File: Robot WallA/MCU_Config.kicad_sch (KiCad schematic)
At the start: 26 parts, among them SW1 Switch

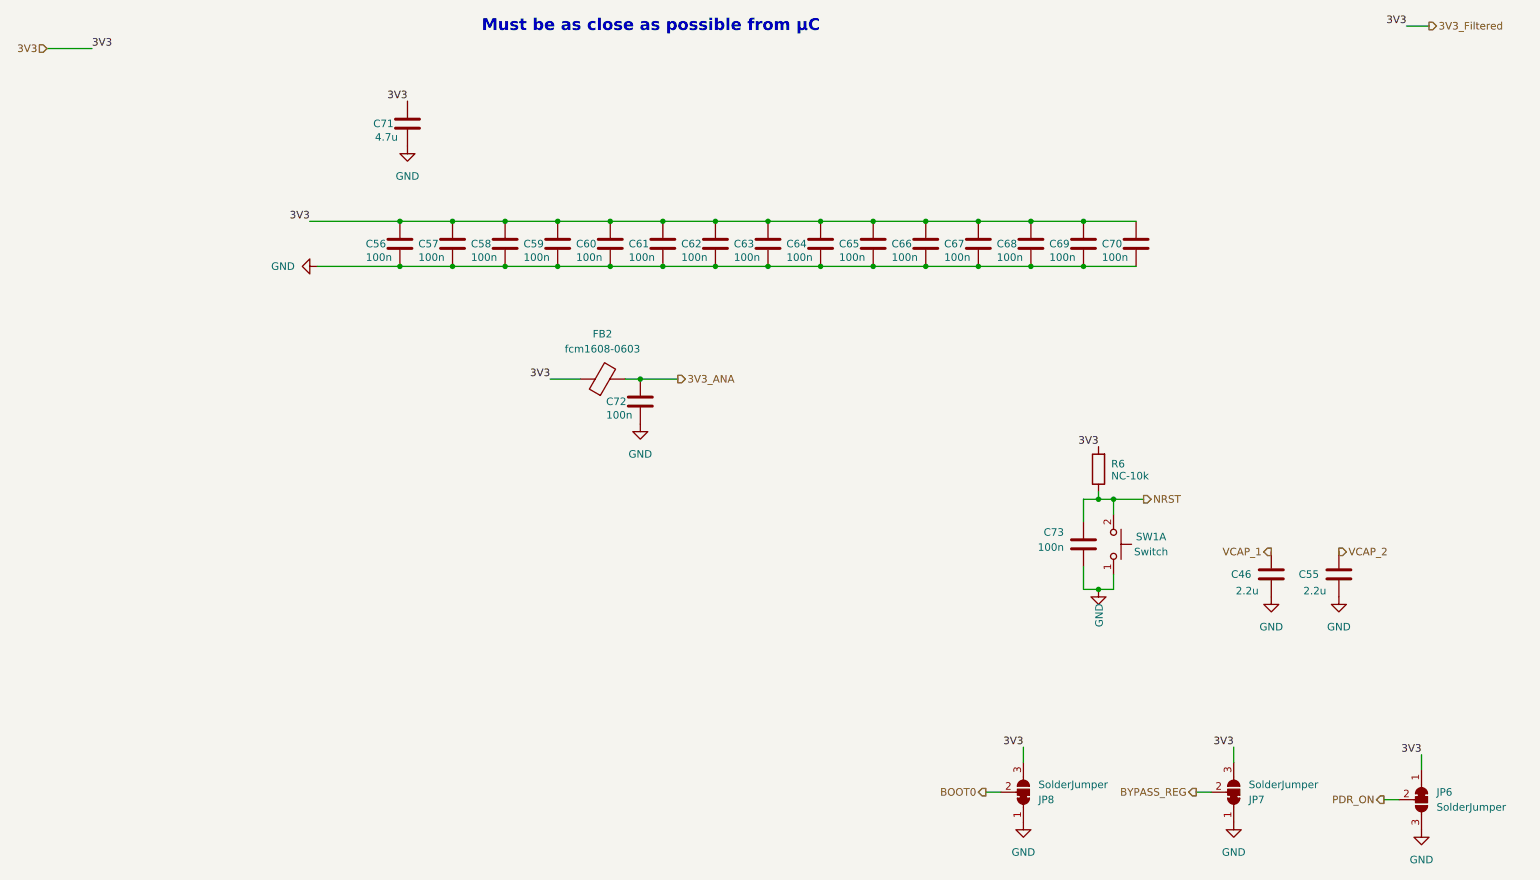
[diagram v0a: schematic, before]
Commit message: Continued to link MCU pins, Added a sheet for servomotors and optional 2 DC motors.
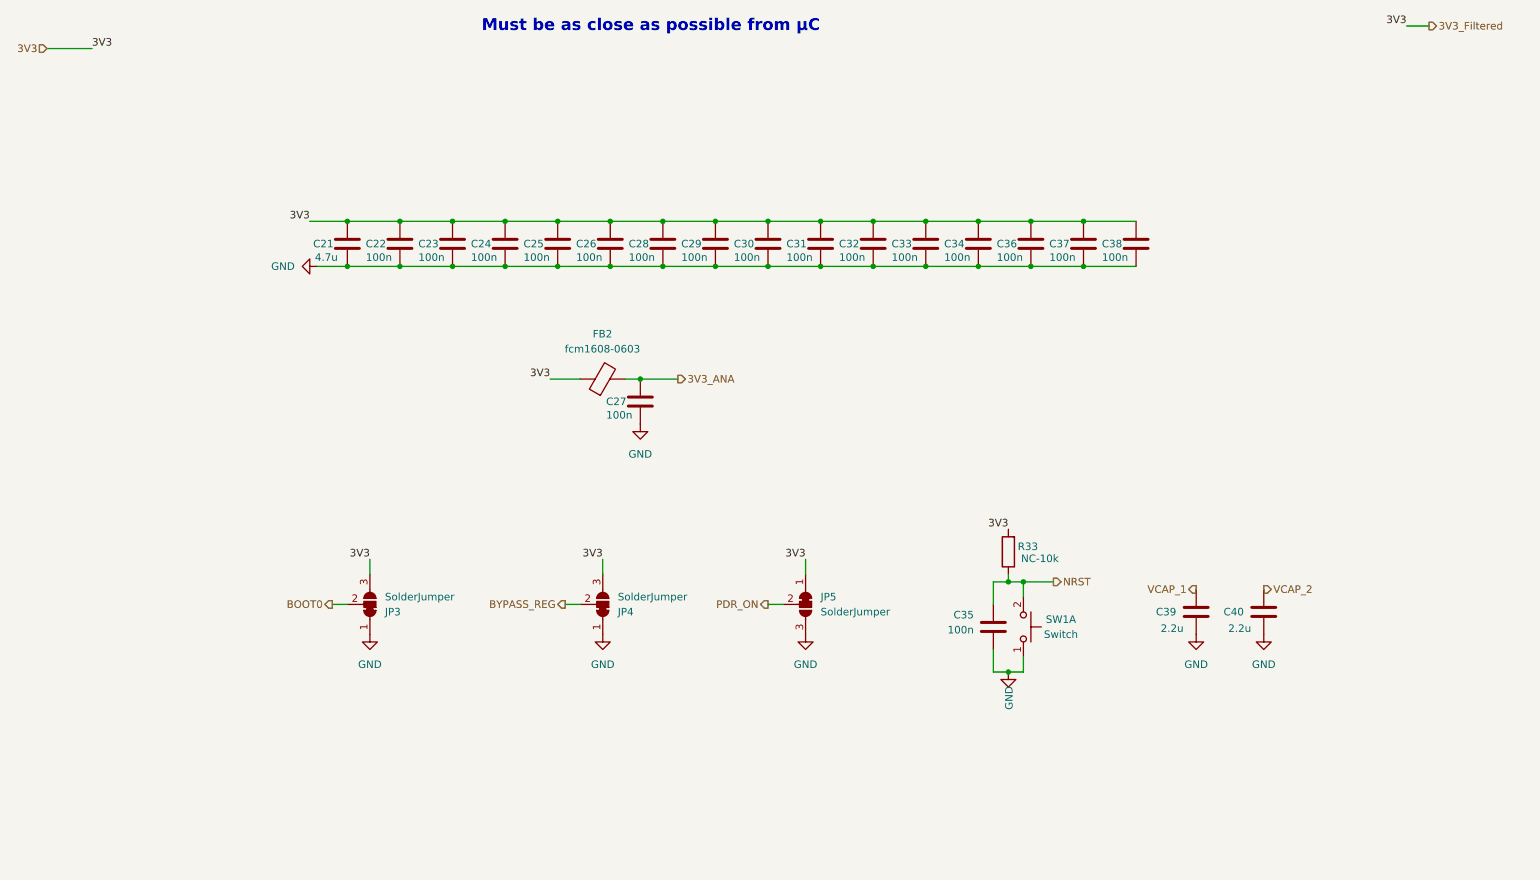
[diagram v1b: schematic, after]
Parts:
- renumbered C71 to C21, C56 to C22, C57 to C23, C58 to C24, C59 to C25, C60 to C26, C72 to C27, C61 to C28, C62 to C29, C63 to C30, C64 to C31, C65 to C32, C66 to C33, C67 to C34, C73 to C35, C68 to C36, C69 to C37, C70 to C38, C46 to C39, C55 to C40, JP8 to JP3, JP7 to JP4, JP6 to JP5, R6 to R33
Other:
- moved on the sheet: C21, C35, C39, C40, JP3, JP4, JP5, R33, SW1A

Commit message: Defined every footprints
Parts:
- C10: renamed from C29; value 100n -> 100nF; footprint (none) -> Capacitor_SMD:C_0603_1608Metric_Pad1.08x0.95mm_HandSolder
- C11: renamed from C30; value 100n -> 100nF; footprint (none) -> Capacitor_SMD:C_0603_1608Metric_Pad1.08x0.95mm_HandSolder
- C12: renamed from C31; value 100n -> 100nF; footprint (none) -> Capacitor_SMD:C_0603_1608Metric_Pad1.08x0.95mm_HandSolder
- C13: renamed from C32; value 100n -> 100nF; footprint (none) -> Capacitor_SMD:C_0603_1608Metric_Pad1.08x0.95mm_HandSolder
- C14: renamed from C33; value 100n -> 100nF; footprint (none) -> Capacitor_SMD:C_0603_1608Metric_Pad1.08x0.95mm_HandSolder
- C15: renamed from C34; value 100n -> 100nF; footprint (none) -> Capacitor_SMD:C_0603_1608Metric_Pad1.08x0.95mm_HandSolder
- C16: renamed from C36; value 100n -> 100nF; footprint (none) -> Capacitor_SMD:C_0603_1608Metric_Pad1.08x0.95mm_HandSolder
- C17: renamed from C37; value 100n -> 100nF; footprint (none) -> Capacitor_SMD:C_0603_1608Metric_Pad1.08x0.95mm_HandSolder
- C18: renamed from C38; value 100n -> 100nF; footprint (none) -> Capacitor_SMD:C_0603_1608Metric_Pad1.08x0.95mm_HandSolder
- C19: renamed from C27; value 100n -> 100nF; footprint (none) -> Capacitor_SMD:C_0603_1608Metric_Pad1.08x0.95mm_HandSolder
- C20: renamed from C39; value 2.2u -> 2.2uF; footprint (none) -> Capacitor_SMD:C_0603_1608Metric_Pad1.08x0.95mm_HandSolder
- C21: renamed from C40; value 2.2u -> 2.2uF; footprint (none) -> Capacitor_SMD:C_0603_1608Metric_Pad1.08x0.95mm_HandSolder
- C22: renamed from C35; value 100n -> 100nF
- C3: renamed from C21; value 4.7u -> 4.7uF; footprint (none) -> Capacitor_SMD:C_0603_1608Metric_Pad1.08x0.95mm_HandSolder
- C4: renamed from C22; value 100n -> 100nF; footprint (none) -> Capacitor_SMD:C_0603_1608Metric_Pad1.08x0.95mm_HandSolder
- C5: renamed from C23; value 100n -> 100nF; footprint (none) -> Capacitor_SMD:C_0603_1608Metric_Pad1.08x0.95mm_HandSolder
- C6: renamed from C24; value 100n -> 100nF; footprint (none) -> Capacitor_SMD:C_0603_1608Metric_Pad1.08x0.95mm_HandSolder
- C7: renamed from C25; value 100n -> 100nF; footprint (none) -> Capacitor_SMD:C_0603_1608Metric_Pad1.08x0.95mm_HandSolder
- C8: renamed from C26; value 100n -> 100nF; footprint (none) -> Capacitor_SMD:C_0603_1608Metric_Pad1.08x0.95mm_HandSolder
- C9: renamed from C28; value 100n -> 100nF; footprint (none) -> Capacitor_SMD:C_0603_1608Metric_Pad1.08x0.95mm_HandSolder
- FB1: renamed from FB2; value fcm1608-0603 -> Bead 600R; footprint (none) -> Resistor_SMD:R_0603_1608Metric_Pad0.98x0.95mm_HandSolder; Manufacturer_Part_Number (none) -> FCM 1608KF-601T03
- JP1: renamed from JP3; footprint Jumper:SolderJumper-3_P1.3mm_Bridged12_RoundedPad1.0x1.5mm -> Jumper:SolderJumper-3_P1.3mm_Bridged12_Pad1.0x1.5mm
- JP2: renamed from JP4; footprint Jumper:SolderJumper-3_P1.3mm_Bridged12_RoundedPad1.0x1.5mm -> Jumper:SolderJumper-3_P1.3mm_Bridged12_Pad1.0x1.5mm
- JP3: renamed from JP5; footprint Jumper:SolderJumper-3_P1.3mm_Bridged12_RoundedPad1.0x1.5mm -> Jumper:SolderJumper-3_P1.3mm_Bridged12_Pad1.0x1.5mm
- R1: renamed from R33; value NC-10k -> 10k; Manufacturer_Part_Number ERJ-3GEYJ103V -> (none); Mouser Reference 667-ERJ-3GEYJ103V -> (none); now not fitted
- SW1: Mouser Reference 611-KMR231NGLFS -> (none)

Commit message: Updated fab files.
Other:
- company: (none) -> Socotec Monitoring
- title: (none) -> Robot Wall-A

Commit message: Modified footprint to simplify BOM. Finalized BOM.
Updated fab files
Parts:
- C10, C11, C12, C13, C14, C15, C16, C17, C18, C19, C22, C4, C5, C6, C7, C8, C9: Manufacturer_Part_Number (none) -> KGM15BR71H104KT
- C20, C21: Manufacturer_Part_Number (none) -> TMK107ABJ225KA-T
- C3: value 4.7uF -> 4.7uF/50V; footprint Capacitor_SMD:C_0603_1608Metric_Pad1.08x0.95mm_HandSolder -> Capacitor_SMD:C_0805_2012Metric_Pad1.18x1.45mm_HandSolder; Manufacturer_Part_Number (none) -> GRM21BR61H475ME51L
- R1: Manufacturer_Part_Number (none) -> 667-ERJ-3GEYJ103V
